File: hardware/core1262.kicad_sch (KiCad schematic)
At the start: 2 parts, among them J1 Conn_Coaxial_Small, U3 CoreSX1262-LF

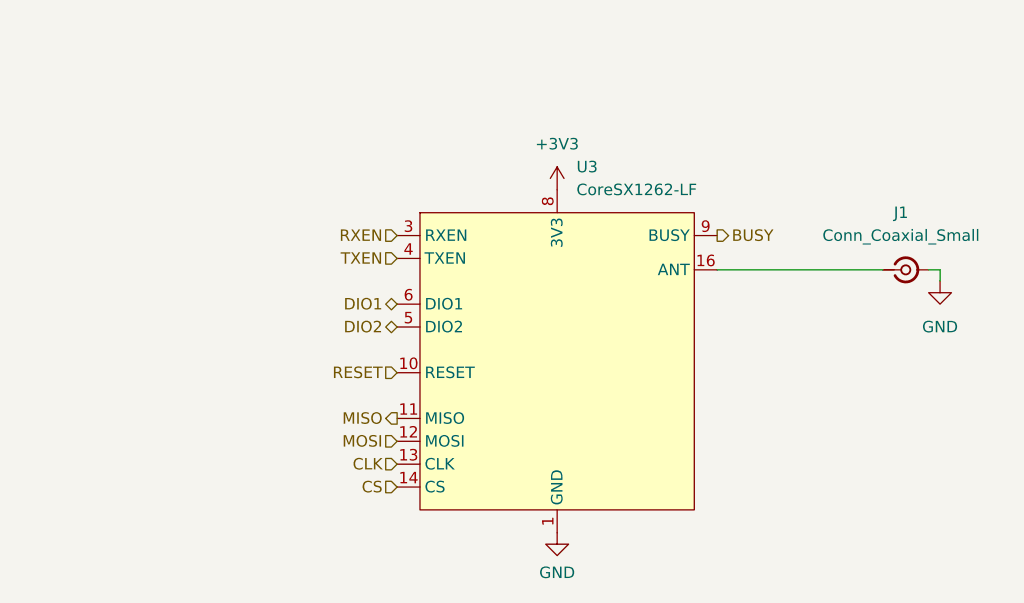
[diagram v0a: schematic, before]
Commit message: drew more busses and connections
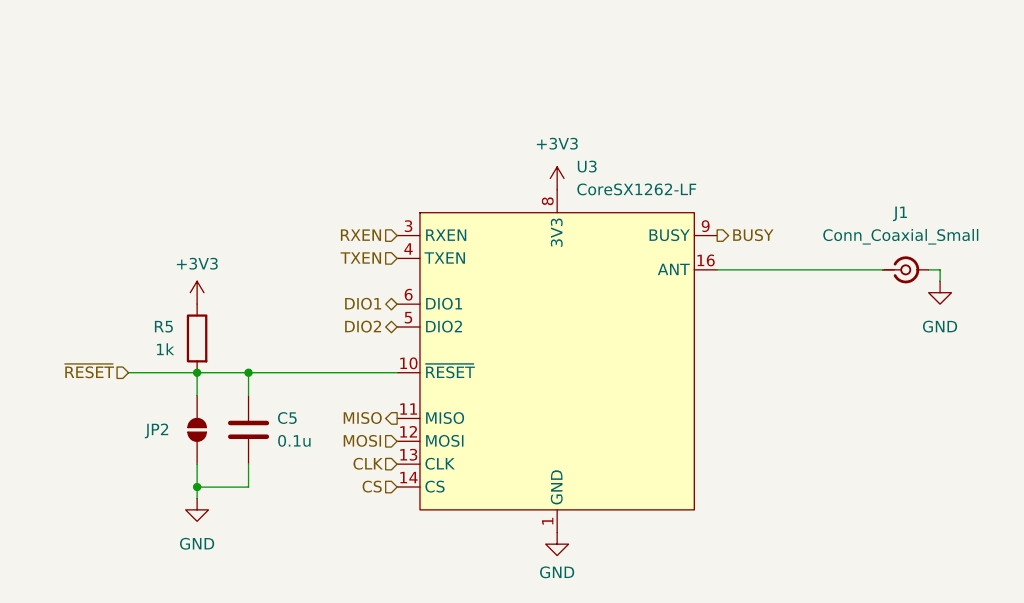
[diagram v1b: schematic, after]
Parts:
- added C5: 0.1u, symbol Device:C
- added JP2: SolderJumper_2_Open, symbol Jumper:SolderJumper_2_Open
- added R5: 1k, symbol Device:R
- U3: Schematic (none) -> https://files.waveshare.com/upload/c/c1/CoreSX1262_Sch.pdf
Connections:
- net +3V3: now also R5.1
- net GND: now also C5.2, JP2.2 (B)
- net RESET renamed ~{RESET}
- net ~{RESET}: now also C5.1, JP2.1 (A), R5.2

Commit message: beginnings of power distribution maybe?
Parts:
- added C8: 22u, symbol Device:C
- added C9: 0.1u, symbol Device:C
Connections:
- net +3V3: now also C8.1, C9.1
- net GND: now also C8.2, C9.2
